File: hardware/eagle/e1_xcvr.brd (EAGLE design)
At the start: 50 x 50 mm, 48 parts, among them T1 BC847C

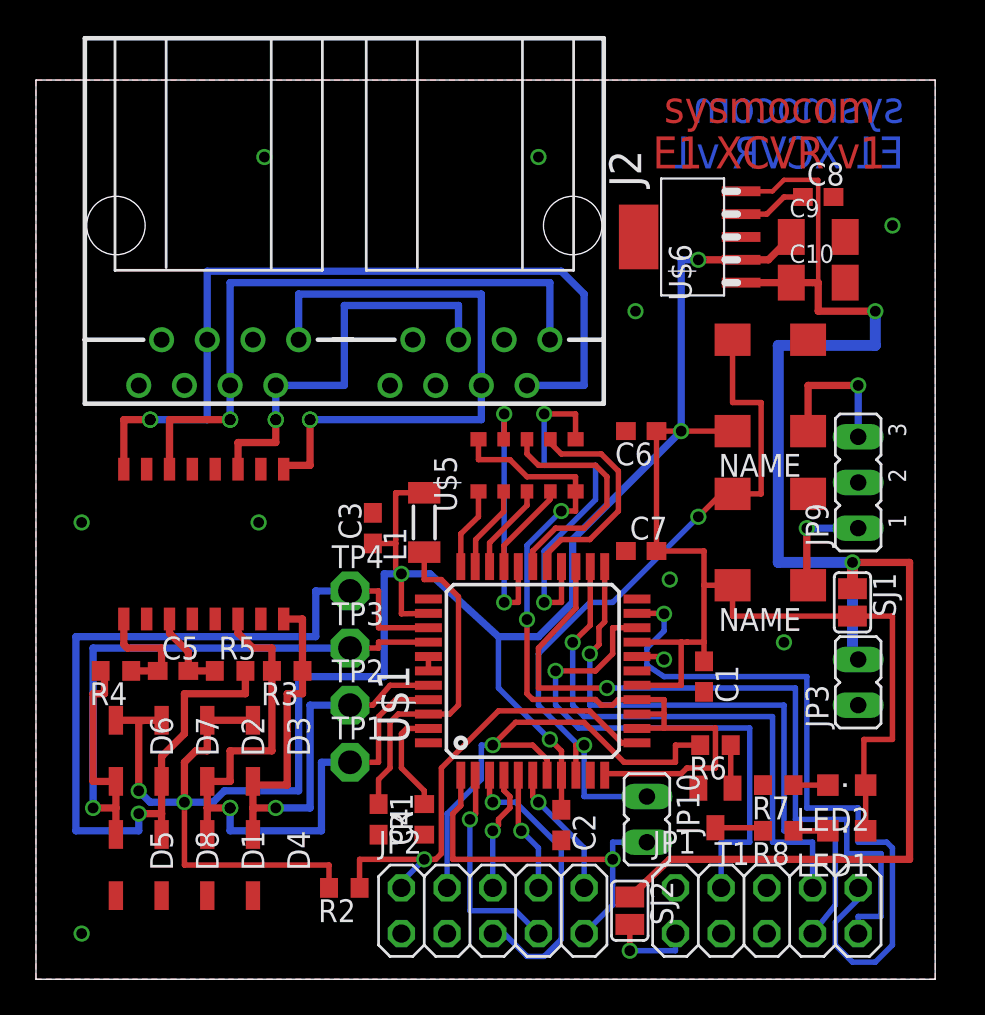
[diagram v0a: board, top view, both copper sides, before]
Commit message: give parts names without "$", use 47nH as L1 (1206)
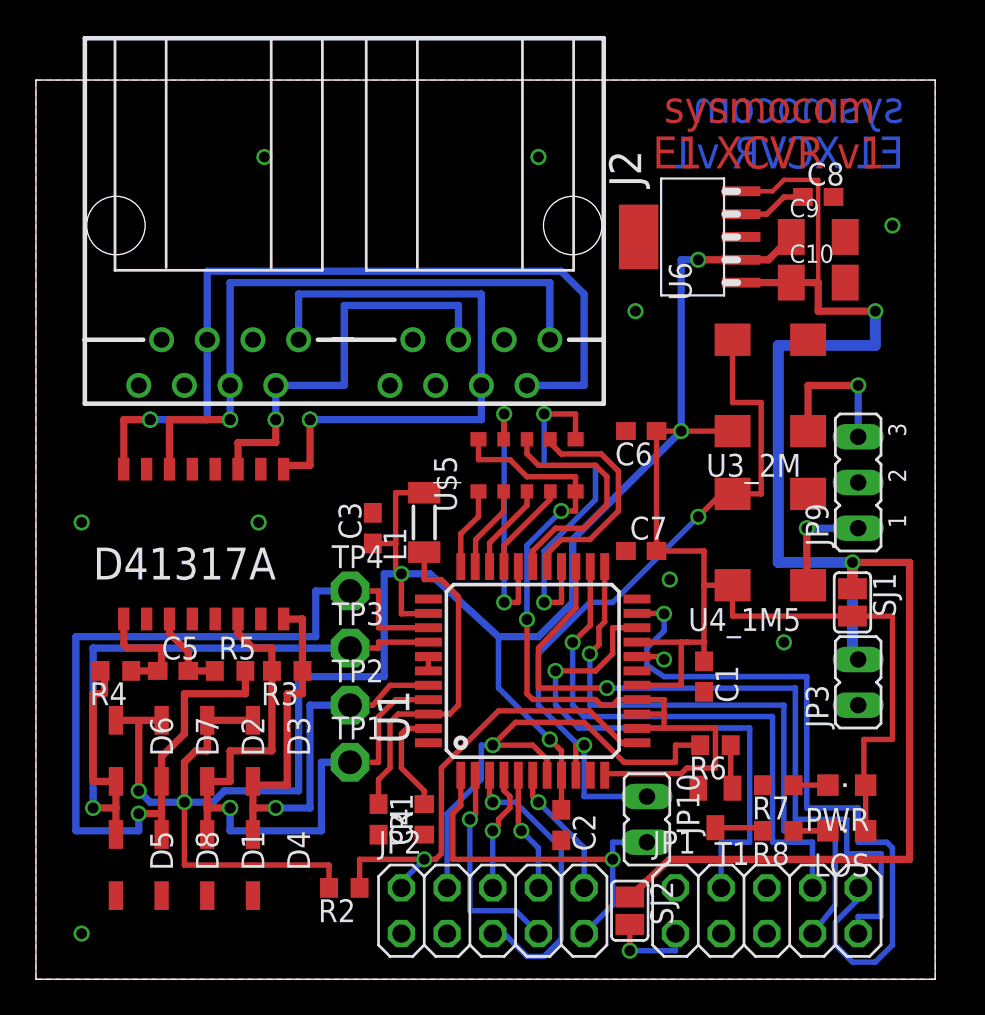
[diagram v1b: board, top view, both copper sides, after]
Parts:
- L1: value (none) -> 47nH
- renumbered LED1 to LOS, LED2 to PWR, U$1 to U1, U$3 to U3_2M, U$4 to U4_1M5, U$6 to U6
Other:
- board text added: "D41317A"

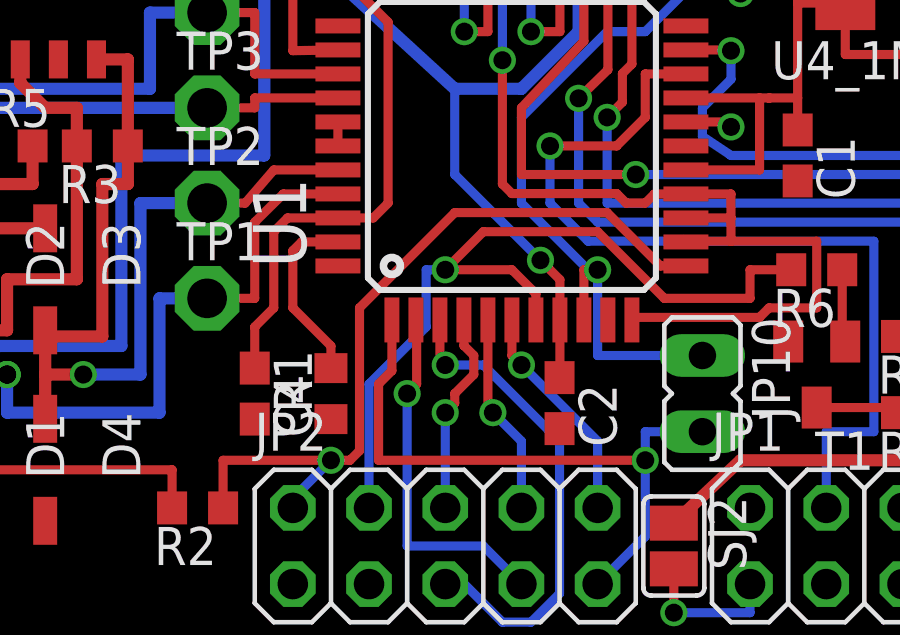
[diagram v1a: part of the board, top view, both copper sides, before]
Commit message: connect LIU's pin 44 to GND (solves OSM#3247)
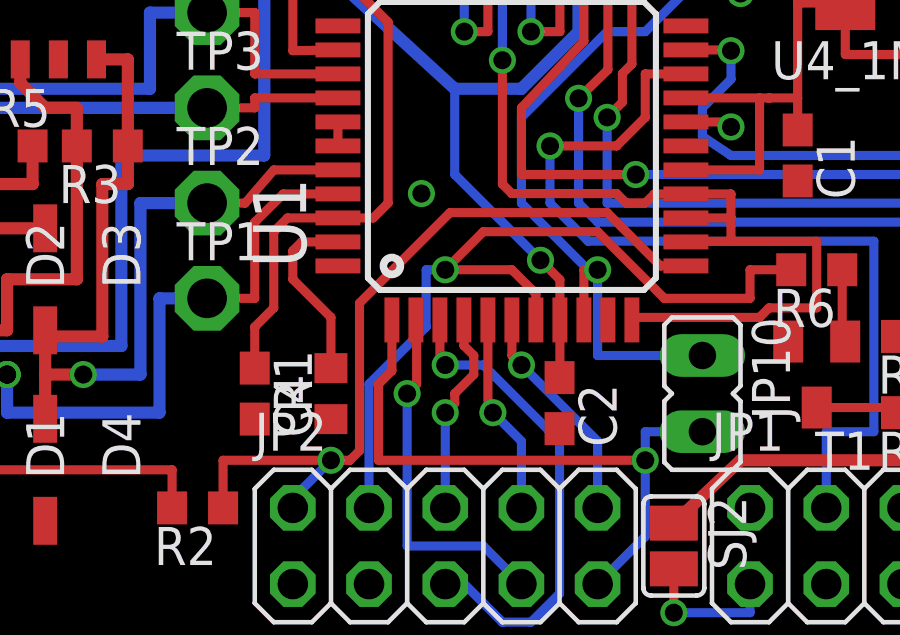
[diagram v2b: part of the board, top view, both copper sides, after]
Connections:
- net GND: now also U1.44
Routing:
- net GND: vias 12 -> 13
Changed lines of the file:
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@@
 <?xml version="1.0" encoding="utf-8"?>
 <!DOCTYPE eagle SYSTEM "eagle.dtd">
-<eagle version="6.0">
+<eagle version="7.6.0">
 <drawing>
 <settings>
@@
 <setting verticaltext="up"/>
 </settings>
-<grid distance="0.3175" unitdist="mm" unit="mm" style="lines" multiple="8" display="yes" altdistance="0.635" altunitdist="mm" altunit="mm"/>
+<grid distance="0.3175" unitdist="mm" unit="mm" style="lines" multiple="1" display="no" altdistance="0.15875" altunitdist="mm" altunit="mm"/>
 <layers>
 <layer number="1" name="Top" color="4" fill="1" visible="yes" active="yes"/>
@@
 <layer number="25" name="tNames" color="7" fill="1" visible="yes" active="yes"/>
 <layer number="26" name="bNames" color="7" fill="1" visible="yes" active="yes"/>
-<layer number="27" name="tValues" color="7" fill="1" visible="yes" active="yes"/>
-<layer number="28" name="bValues" color="7" fill="1" visible="yes" active="yes"/>
+<layer number="27" name="tValues" color="7" fill="1" visible="no" active="yes"/>
+<layer number="28" name="bValues" color="7" fill="1" visible="no" active="yes"/>
 <layer number="29" name="tStop" color="7" fill="3" visible="yes" active="yes"/>
 <layer number="30" name="bStop" color="7" fill="6" visible="yes" active="yes"/>
@@
 <layer number="33" name="tFinish" color="6" fill="3" visible="yes" active="yes"/>
 <layer number="34" name="bFinish" color="6" fill="6" visible="yes" active="yes"/>
-<layer number="35" name="tGlue" color="7" fill="4" visible="yes" active="yes"/>
-<layer number="36" name="bGlue" color="7" fill="5" visible="yes" active="yes"/>
-<layer number="37" name="tTest" color="7" fill="1" visible="yes" active="yes"/>
-<layer number="38" name="bTest" color="7" fill="1" visible="yes" active="yes"/>
-<layer number="39" name="tKeepout" color="4" fill="11" visible="yes" active="yes"/>
-<layer number="40" name="bKeepout" color="1" fill="11" visible="yes" active="yes"/>
-<layer number="41" name="tRestrict" color="4" fill="10" visible="yes" active="yes"/>
-<layer number="42" name="bRestrict" color="1" fill="10" visible="yes" active="yes"/>
-<layer number="43" name="vRestrict" color="2" fill="10" visible="yes" active="yes"/>
-<layer number="44" name="Drills" color="7" fill="1" visible="yes" active="yes"/>
-<layer number="45" name="Holes" color="7" fill="1" visible="yes" active="yes"/>
-<layer number="46" name="Milling" color="3" fill="1" visible="yes" active="yes"/>
+<layer number="35" name="tGlue" color="7" fill="4" visible="no" active="yes"/>
+<layer number="36" name="bGlue" color="7" fill="5" visible="no" active="yes"/>
+<layer number="37" name="tTest" color="7" fill="1" visible="no" active="yes"/>
+<layer number="38" name="bTest" color="7" fill="1" visible="no" active="yes"/>
+<layer number="39" name="tKeepout" color="4" fill="11" visible="no" active="yes"/>
+<layer number="40" name="bKeepout" color="1" fill="11" visible="no" active="yes"/>
+<layer number="41" name="tRestrict" color="4" fill="10" visible="no" active="yes"/>
+<layer number="42" name="bRestrict" color="1" fill="10" visible="no" active="yes"/>
+<layer number="43" name="vRestrict" color="2" fill="10" visible="no" active="yes"/>
+<layer number="44" name="Drills" color="7" fill="1" visible="no" active="yes"/>
+<layer number="45" name="Holes" color="7" fill="1" visible="no" active="yes"/>
+<layer number="46" name="Milling" color="3" fill="1" visible="no" active="yes"/>
 <layer number="47" name="Measures" color="7" fill="1" visible="yes" active="yes"/>
 <layer number="48" name="Document" color="7" fill="1" visible="yes" active="yes"/>
 <layer number="49" name="Reference" color="7" fill="1" visible="yes" active="yes"/>
-<layer number="51" name="tDocu" color="7" fill="1" visible="yes" active="yes"/>
-<layer number="52" name="bDocu" color="7" fill="1" visible="yes" active="yes"/>
+<layer number="51" name="tDocu" color="7" fill="1" visible="no" active="yes"/>
+<layer number="52" name="bDocu" color="7" fill="1" visible="no" active="yes"/>
 <layer number="91" name="Nets" color="2" fill="1" visible="no" active="no"/>
 <layer number="92" name="Busses" color="1" fill="1" visible="no" active="no"/>
@@
 </class>
 </classes>
-<designrules>
+<designrules name="default">
 <description language="de">&lt;b&gt;EAGLE Design Rules&lt;/b&gt;
 &lt;p&gt;
@@
 <pass name="Default">
 <param name="RoutingGrid" value="5mil"/>
+<param name="AutoGrid" value="1"/>
+<param name="Efforts" value="0"/>
+<param name="TopRouterVariant" value="1"/>
 <param name="tpViaShape" value="round"/>
 <param name="PrefDir.1" value="|"/>
@@
 <wire x1="30.005" y1="26.035" x2="30.005" y2="27.125" width="0.3048" layer="1"/>
 <wire x1="31.7075" y1="11.43" x2="35.8775" y2="11.43" width="0.3048" layer="1"/>
+<contactref element="U1" pad="44"/>
+<via x="24.60625" y="15.5575" extent="1-16" drill="0.6"/>
 </signal>
 <signal name="N$1">
@@
 <wire x1="21.8225" y1="13.945" x2="20.6125" y2="13.945" width="0.3048" layer="1"/>
 <wire x1="20.6125" y1="13.945" x2="20.32" y2="13.6525" width="0.3048" layer="1"/>
-<wire x1="20.32" y1="13.6525" x2="20.32" y2="11.7475" width="0.3048" layer="1"/>
-<wire x1="20.32" y1="11.7475" x2="21.59" y2="10.4775" width="0.3048" layer="1"/>
-<wire x1="21.59" y1="10.4775" x2="21.59" y2="9.74" width="0.3048" layer="1"/>
+<wire x1="20.32" y1="13.6525" x2="20.32" y2="12.7" width="0.3048" layer="1"/>
+<wire x1="20.32" y1="12.7" x2="21.59" y2="11.43" width="0.3048" layer="1"/>
+<wire x1="21.59" y1="11.43" x2="21.59" y2="9.74" width="0.3048" layer="1"/>
 </signal>
 <signal name="VDD" class="1">
@@
 <wire x1="33.4225" y1="13.145" x2="32.575" y2="13.145" width="0.3048" layer="1"/>
 <wire x1="32.575" y1="13.145" x2="30.7975" y2="14.9225" width="0.3048" layer="1"/>
-<wire x1="30.7975" y1="14.9225" x2="25.7175" y2="14.9225" width="0.3048" layer="1"/>
-<wire x1="25.7175" y1="14.9225" x2="22.5425" y2="11.7475" width="0.3048" layer="1"/>
-<wire x1="22.5425" y1="11.7475" x2="22.5425" y2="6.985" width="0.3048" layer="1"/>
+<wire x1="30.7975" y1="14.9225" x2="25.55875" y2="14.9225" width="0.3048" layer="1"/>
+<wire x1="25.55875" y1="14.9225" x2="22.5425" y2="11.90625" width="0.3048" layer="1"/>
+<wire x1="22.5425" y1="11.90625" x2="22.5425" y2="6.985" width="0.3048" layer="1"/>
 <wire x1="22.5425" y1="6.985" x2="22.225" y2="6.6675" width="0.3048" layer="1"/>
 <wire x1="22.225" y1="6.6675" x2="21.59" y2="6.6675" width="0.3048" layer="1"/>

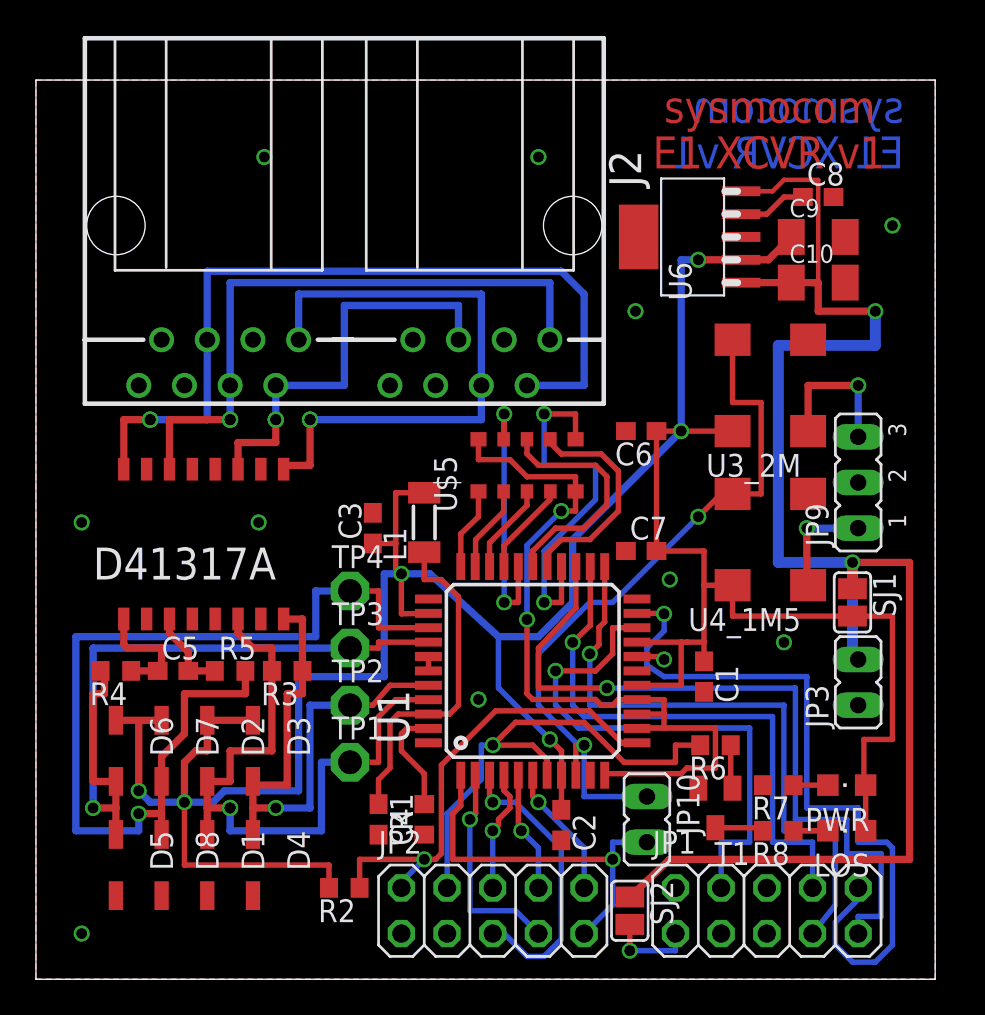
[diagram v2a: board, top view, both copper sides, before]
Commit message: replace old PULSE_T1094NL footprint, repair pin assignment (solves OSM#3269)
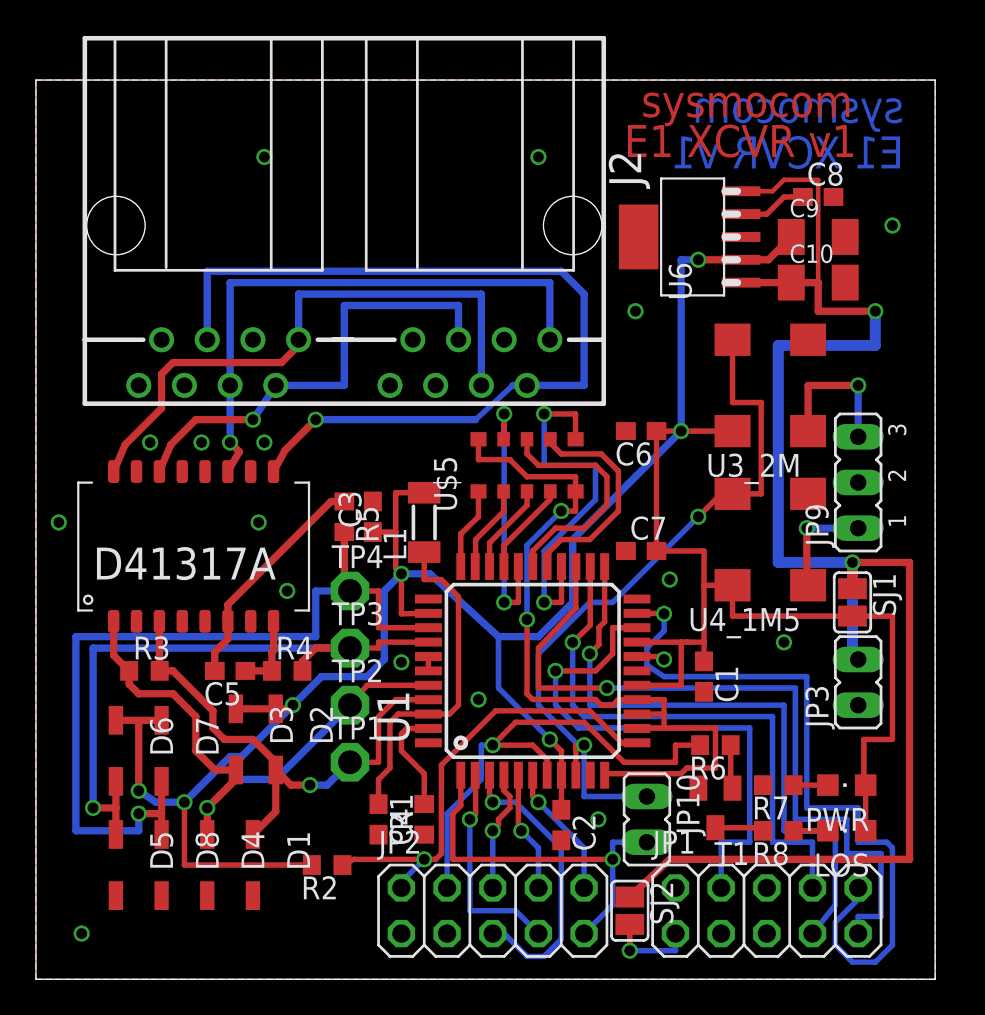
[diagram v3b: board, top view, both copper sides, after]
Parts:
- moved R5 10.7 mm to (17.1, 25.7), turned to 270 degrees
- moved R4 9.53 mm to (14.0, 17.1), turned to 0 degrees
- moved R3 7.94 mm to (6.03, 17.1), turned to 0 degrees
- moved D2 3.86 mm to (13.3, 13.3)
- moved C5 3.17 mm to (10.8, 17.1), turned to 180 degrees
- moved D1 2.54 mm to (12.1, 6.35)
- moved D4 2.54 mm to (9.53, 6.35)
- moved R2 1.59 mm to (16.2, 6.35)
- moved D3 1.14 mm to (11.1, 13.3)
- moved U$2 0.95 mm to (8.57, 24.1), turned to 90 degrees
- moved C3 0.64 mm to (18.7, 25.7)
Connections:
- net N$29: now also U$2.8; no longer U$2.P$8
- net N$31: now also U$2.6; no longer U$2.P$6
- net N$32: now also U$2.9; no longer U$2.P$9
- net N$34: now also U$2.16; no longer U$2.P$16
- net N$36: now also U$2.11; no longer U$2.P$11
- net N$40: now also U$2.14; no longer U$2.P$14
- net RRING: now also U$2.1; no longer U$2.P$1
- net RTIP: now also U$2.3; no longer U$2.P$3
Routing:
- net VDD: track 172.0 -> 160.1 mm, vias 6 -> 7
- net RTIP: track 37.3 -> 28.7 mm, vias 2 -> 1
- net N$31: track 4.79 -> 12.8 mm
- net TRING: track 53.7 -> 47.1 mm
- net TTIP: track 40.5 -> 35.6 mm
- net N$32: track 45.4 -> 49.8 mm, vias 2 -> 1
- net N$36: track 34.7 -> 31.8 mm, vias 2 -> 1
- net N$40: track 23.3 -> 25.6 mm, vias 2 -> 1
- net N$29: track 6.56 -> 4.27 mm
- net N$34: track 33.4 -> 32.8 mm, vias 2 -> 0
- net N$17: track 26.2 -> 25.6 mm
- net GND: vias 13 -> 19
